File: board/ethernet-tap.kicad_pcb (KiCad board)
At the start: 4 copper layers, 399 parts, among them J1 BARREL_JACK, J10 XILINX_JTAG, J2 BEL_FUSE_0826-1G1T-23-F, J3 JUMPER_0402_SPDT, J4 JUMPER_0402_SPDT, J5 RJ45, J6 BEL_FUSE_0826-1G1T-23-F, J7 BEL_FUSE_0826-1G1T-23-F, J8 BEL_FUSE_0826-1G1T-23-F, J9 XILINX_JTAG, SW1 SWITCH, SW2 SWITCH, SW3 SWITCH, SW4 SWITCH, SW5 SWITCH, SW6 SWITCH, SW7 BUTTON, U1 LTC3374-QFN, U10 ECS-2016MVQ-250-CN-TR, U11 ECS-2016MVQ-250-CN-TR, U12 ECS-2016MVQ-250-CN-TR, U13 STM32H735-UFBGA176-25, U14 S25FLxxxS_BGA24_5x5_VIO, U2 KSZ9031RN, U3 MAX232, U4 XC7S15-1FTGB196C, U5 KSZ9031RN, U6 KSZ9031RN, U7 ECS-2016MVQ-250-CN-TR, U8 ECS-2016MVQ-250-CN-TR, U9 KSZ9031RN

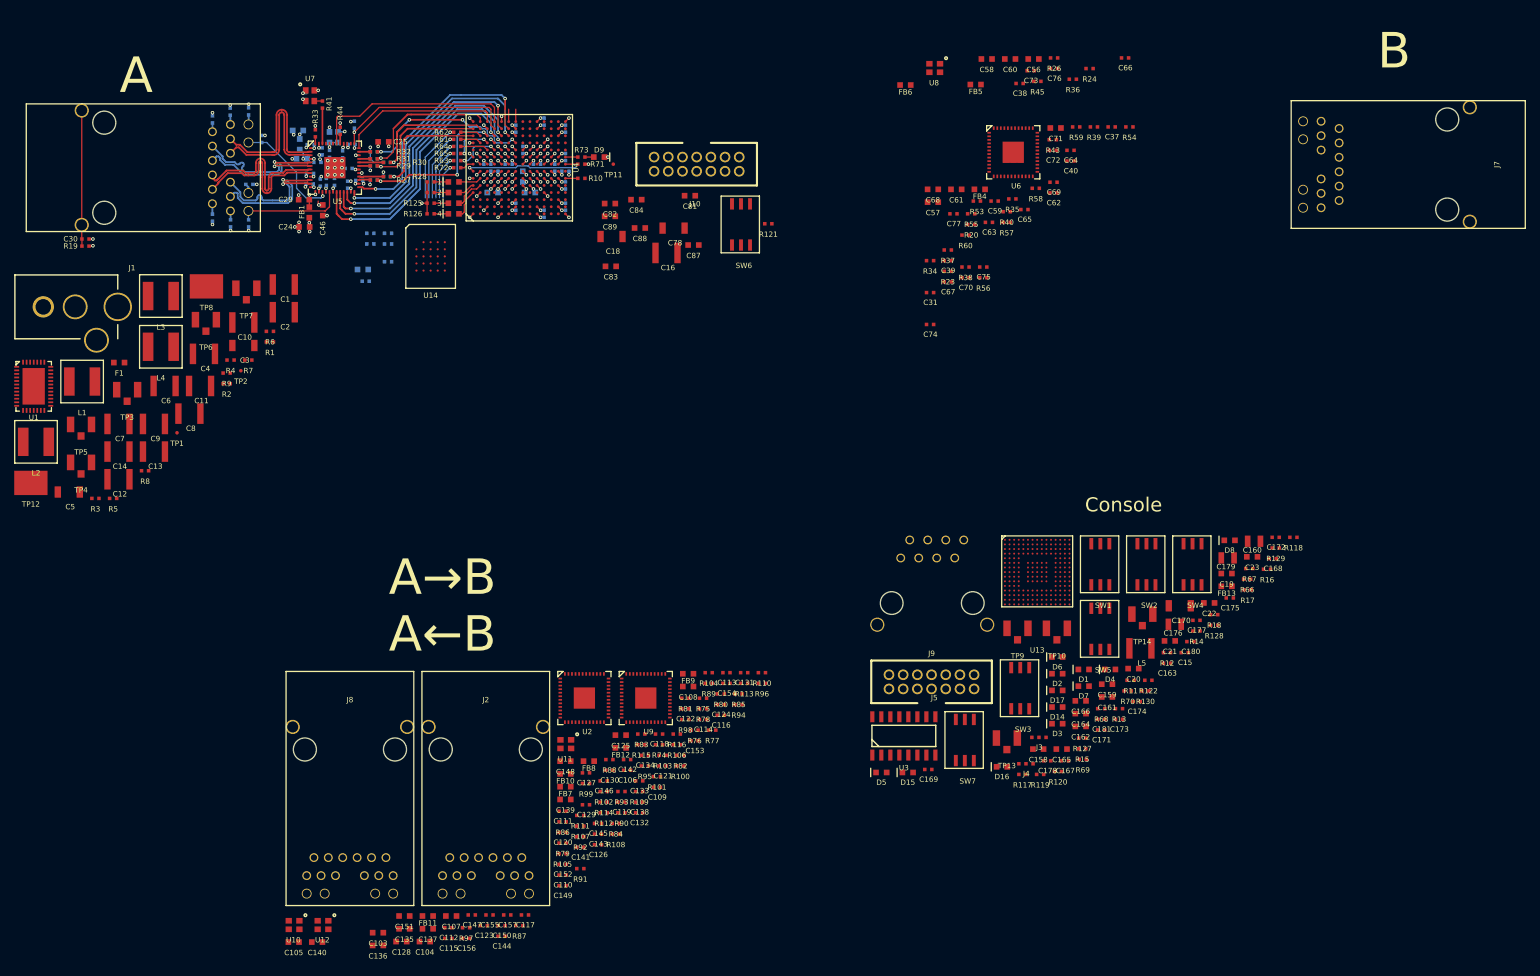
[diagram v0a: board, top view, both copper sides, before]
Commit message: Good progress hooking up second PHY
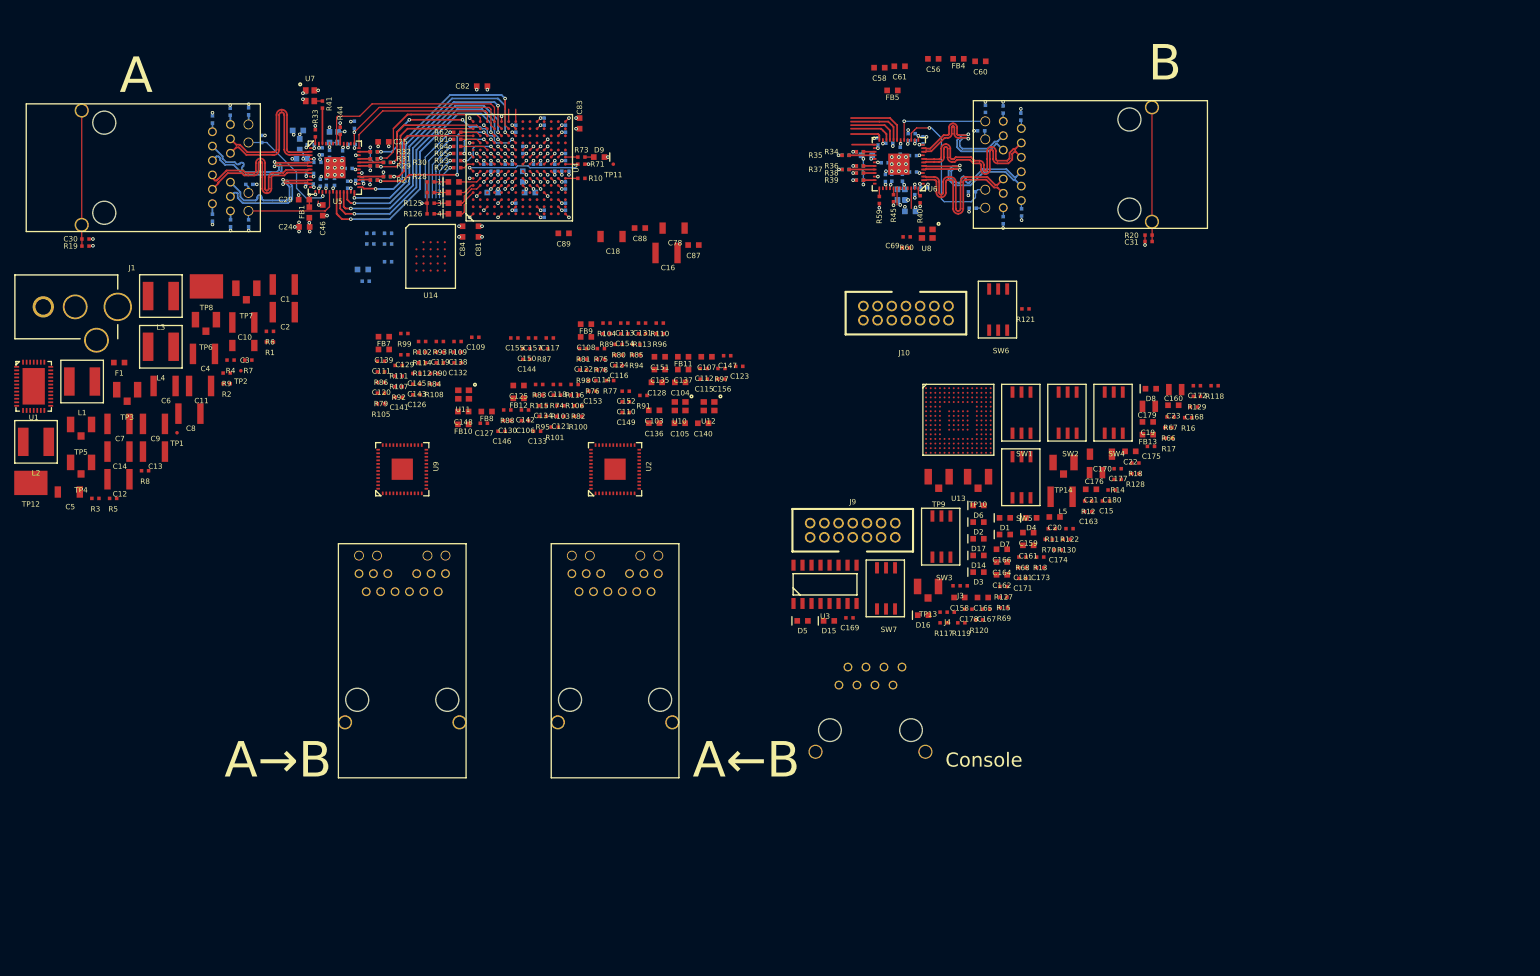
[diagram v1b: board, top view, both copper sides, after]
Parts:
- C37, C38, C39, C40, C57, C59, C62, C63, C64, C65, C66, C67, C68, C70, C71, C72, C73, C74, C75, C76, C77, FB6, R23, R24, R26, R43, R53, R54, R55, R56, R57, R58: moved to B.Cu
- moved C105 91.2 mm to (111.6, 75.0)
- moved C140 91.2 mm to (114.9, 75.0)
- moved U10 91.2 mm to (111.7, 72.6)
- moved U12 91.2 mm to (115.8, 72.6)
- moved C112 86.7 mm to (115.0, 67.3)
- moved C115 86.7 mm to (115.0, 68.8)
- moved C135 86.7 mm to (108.8, 67.5)
- moved C137 86.7 mm to (112.1, 67.5)
- moved C156 86.7 mm to (117.5, 68.8)
- moved R97 86.7 mm to (117.5, 67.3)
- moved C104 86.7 mm to (111.7, 69.2)
- moved C123 86.7 mm to (120.0, 67.0)
- moved C128 86.7 mm to (108.4, 69.2)
- moved C147 86.7 mm to (118.3, 65.5)
- moved C107 86.7 mm to (115.4, 65.7)
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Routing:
- net /GND: track 342.5 -> 481.9 mm, vias 102 -> 135
- net /3V3: track 154.4 -> 242.9 mm, vias 26 -> 37
- net /1V2: track 36.5 -> 66.2 mm, vias 9 -> 17
- net /Thru Path/ETH1_A_P: track 0.00 -> 24.8 mm
- net /Thru Path/ETH1_A_N: track 0.00 -> 24.8 mm
- net /Thru Path/ETH1_C_P: track 0.00 -> 24.8 mm
- net /Thru Path/ETH1_C_N: track 0.00 -> 24.8 mm
- net /Thru Path/ETH1_LED2_N: track 0.00 -> 22.2 mm, vias 0 -> 1
- net /Thru Path/ETH1_B_N: track 0.00 -> 20.7 mm, vias 0 -> 1
- net /Thru Path/ETH1_B_P: track 0.00 -> 20.6 mm, vias 0 -> 1
- net /Thru Path/ETH1_D_N: track 0.00 -> 20.3 mm, vias 0 -> 1
- net /Thru Path/ETH1_D_P: track 0.00 -> 19.1 mm, vias 0 -> 1
- net Net-(C31-Pad2): track 0.00 -> 18.9 mm
- net /Thru Path/ETH1_LED1_N: track 0.00 -> 14.1 mm, vias 0 -> 1
- net /Thru Path/ETH1_A3V3: track 0.00 -> 9.28 mm, vias 0 -> 3
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
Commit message: Continued initial layout. Good progress on monitor port PHYs.
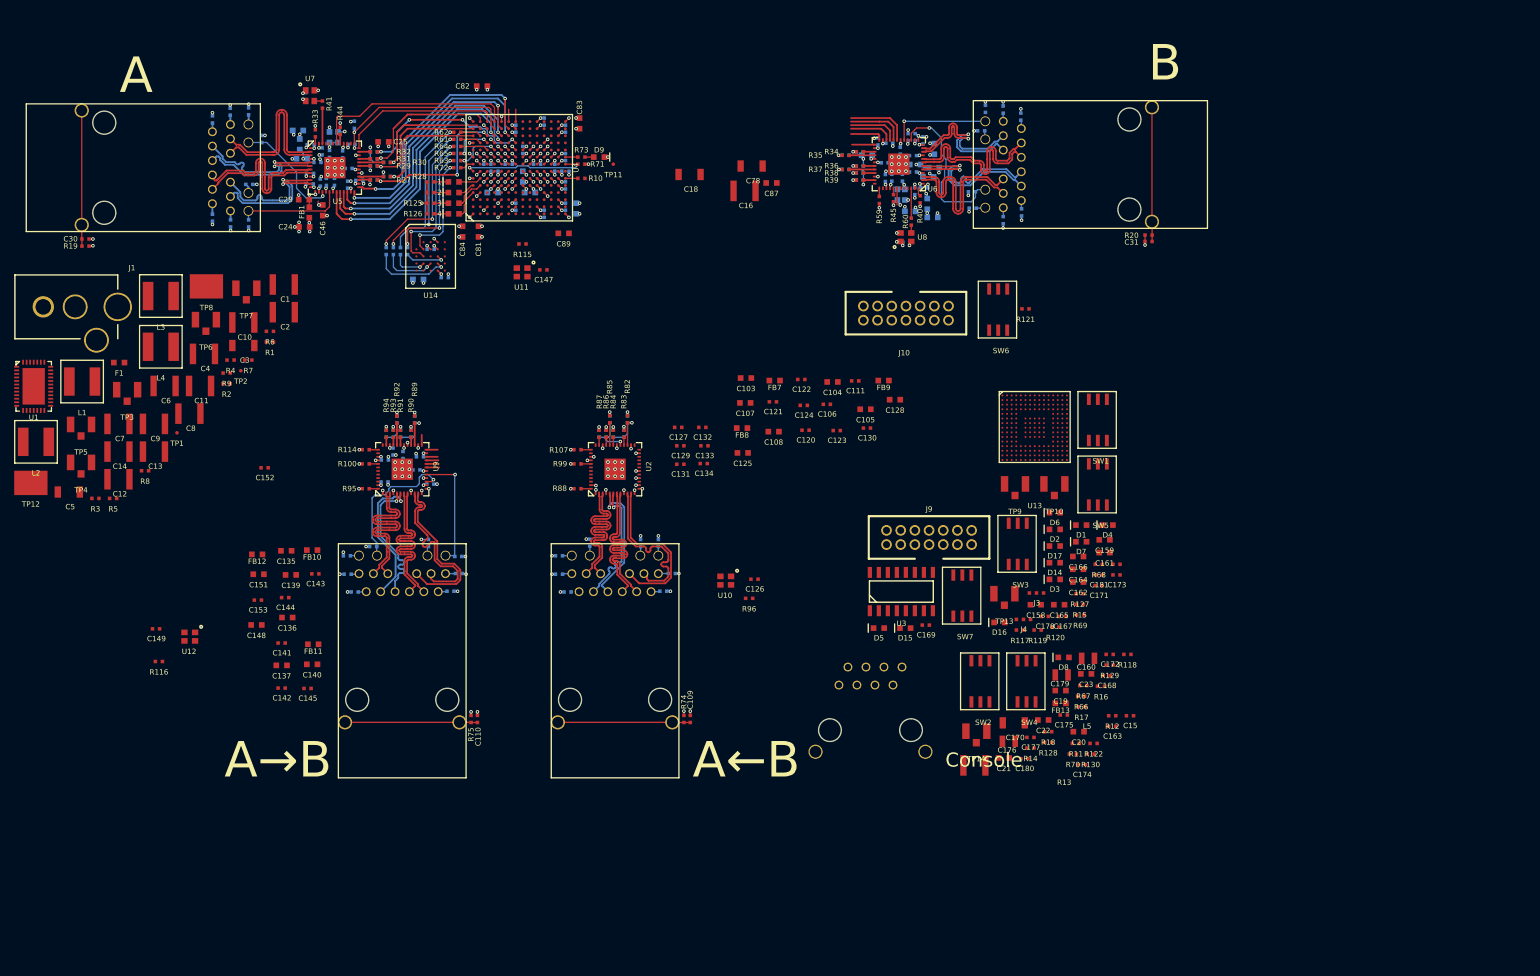
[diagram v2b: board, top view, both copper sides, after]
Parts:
- C112, C113, C114, C115, C116, C117, C118, C119, C138, C146, C150, C154, C155, C156, C157, C56, C58, C60, C61, C69, C88, FB4, FB5, R101, R102, R103, R104, R105, R106, R108, R109, R110, R111, R112, R113, R76, R77, R78, R79, R80, R81, R97, R98: moved to B.Cu
- moved U12 80.1 mm to (42.5, 105.1)
- moved C149 72.9 mm to (37.8, 104.0)
- moved R116 70.4 mm to (38.2, 108.6)
- moved C137 70.3 mm to (55.5, 109.2)
- moved C111 66.9 mm to (136.3, 69.0)
- moved FB11 66.0 mm to (60.0, 106.2)
- moved C140 64.8 mm to (59.8, 109.0)
- moved C151 64.3 mm to (52.2, 96.3)
- moved C109 61.7 mm to (113.1, 116.7), turned to -90 degrees
- moved C120 60.2 mm to (129.3, 76.0)
- moved C135 58.5 mm to (56.1, 93.0)
- moved C136 58.5 mm to (56.3, 102.4)
- moved C153 55.6 mm to (52.1, 100.0)
- moved FB7 55.4 mm to (125.0, 69.0)
- moved R75 55.3 mm to (82.2, 116.7), turned to -90 degrees
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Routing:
- net /GND: track 481.9 -> 698.7 mm, vias 135 -> 188
- net /3V3: track 242.9 -> 390.2 mm, vias 37 -> 63
- net /1V2: track 66.2 -> 110.9 mm, vias 17 -> 30
- net /Monitor Path/ETH3_D_N: track 0.00 -> 24.0 mm
- net /Monitor Path/ETH3_D_P: track 0.00 -> 24.0 mm
- net /Monitor Path/ETH3_A_P: track 0.00 -> 23.9 mm
- net /Monitor Path/ETH3_A_N: track 0.00 -> 23.9 mm
- net /Monitor Path/ETH3_C_N: track 0.00 -> 23.9 mm
- net /Monitor Path/ETH3_C_P: track 0.00 -> 23.9 mm
- net /Monitor Path/ETH2_D_N: track 0.00 -> 23.1 mm
- net /Monitor Path/ETH2_D_P: track 0.00 -> 23.0 mm
- net /Monitor Path/ETH2_C_N: track 0.00 -> 22.9 mm
- net /Monitor Path/ETH2_C_P: track 0.00 -> 22.9 mm
- net /Monitor Path/ETH2_A_P: track 0.00 -> 22.9 mm
- net /Monitor Path/ETH2_A_N: track 0.00 -> 22.9 mm
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
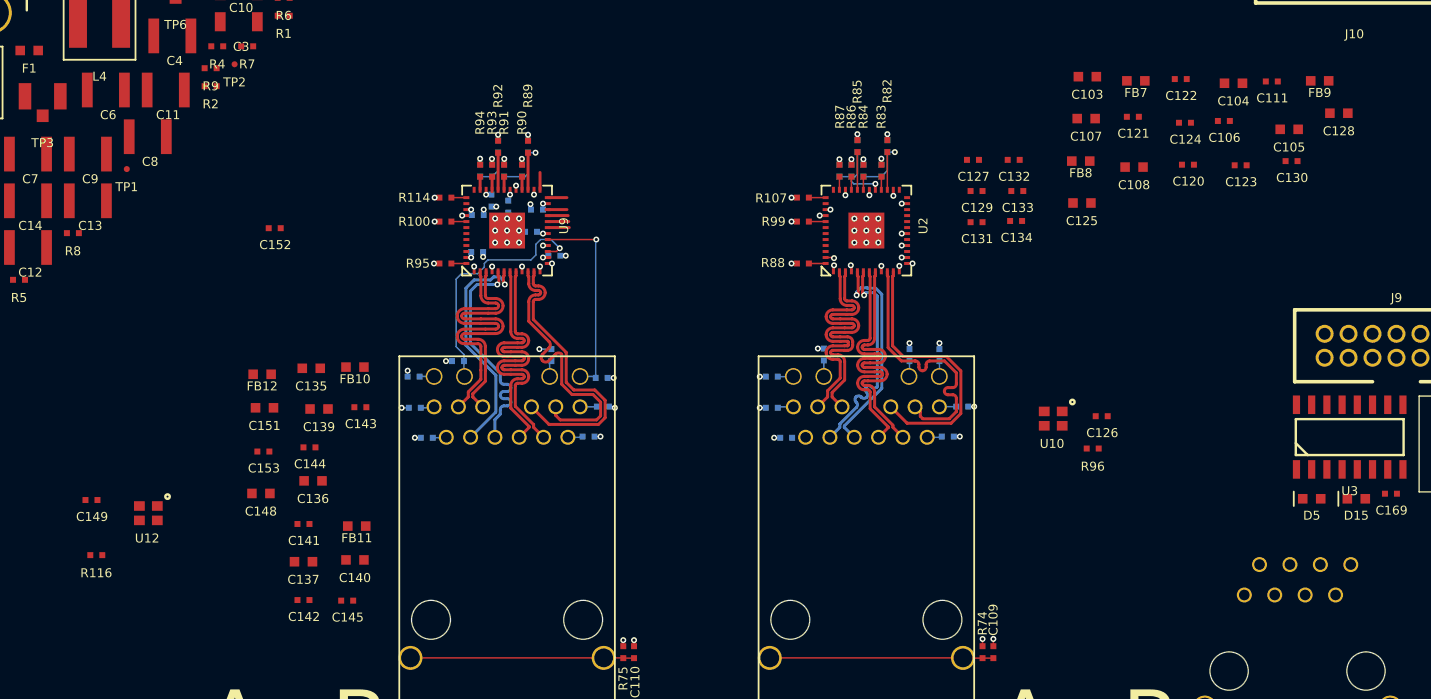
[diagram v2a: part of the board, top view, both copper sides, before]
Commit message: Continued work on monitor port PHY layout
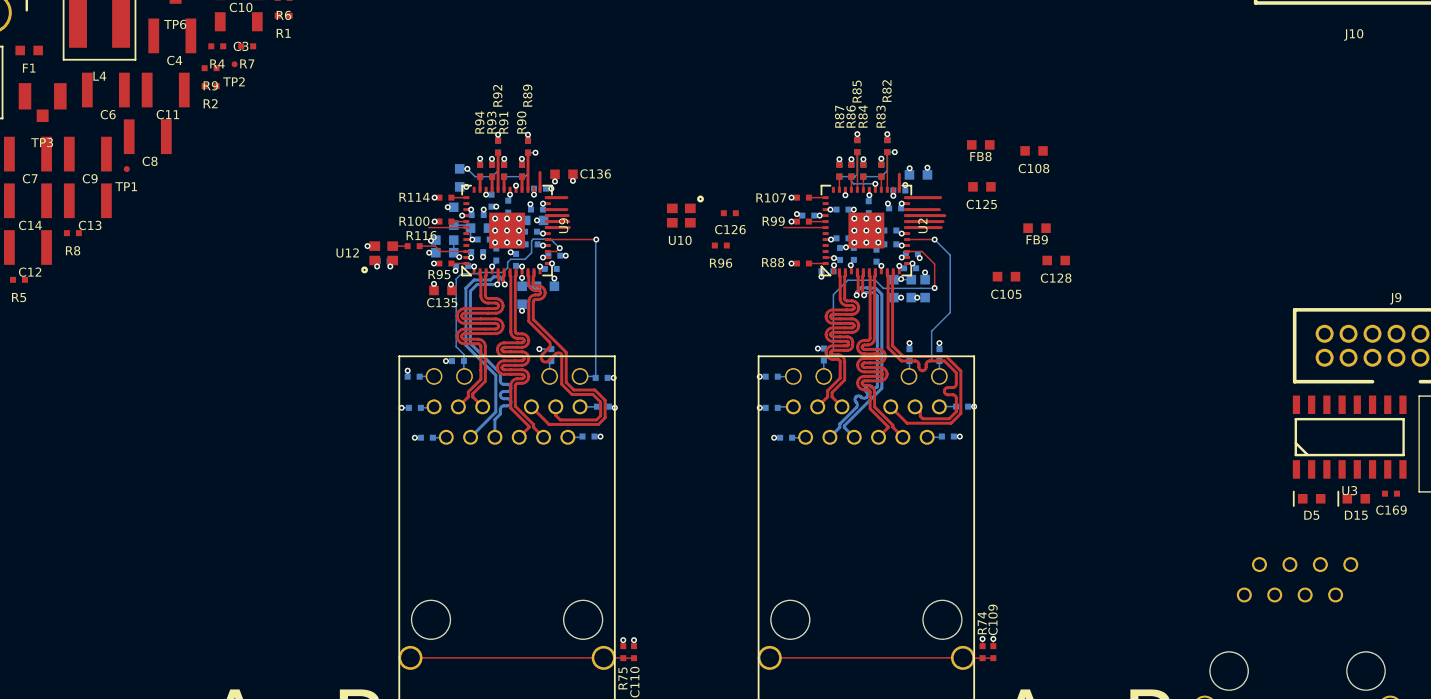
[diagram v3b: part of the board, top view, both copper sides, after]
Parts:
- C103, C104, C106, C107, C111, C120, C121, C122, C123, C124, C127, C129, C130, C131, C132, C133, C134, C137, C139, C140, C141, C142, C143, C144, C145, C148, C149, C151, C152, C153, FB10, FB11, FB12, FB7: moved to B.Cu
- moved C111 40.3 mm to (97.7, 80.2), turned to 180 degrees
- moved C130 38.1 mm to (100.5, 82.2)
- moved R116 37.0 mm to (64.7, 82.8), turned to 180 degrees
- moved C126 35.4 mm to (91.1, 80.0)
- moved R96 35.4 mm to (90.3, 82.8)
- moved U10 35.4 mm to (87.0, 80.2)
- moved C137 34.6 mm to (68.5, 77.1), turned to 90 degrees
- moved C122 33.6 mm to (99.2, 84.9), turned to 180 degrees
- moved C142 33.5 mm to (73.2, 84.0), turned to 90 degrees
- moved C123 33.1 mm to (101.5, 83.5), turned to 90 degrees
- moved C136 33.1 mm to (77.2, 76.8)
- moved C148 32.3 mm to (74.8, 80.7), turned to 180 degrees
- moved C149 31.5 mm to (62.2, 84.0)
- moved C145 31.5 mm to (71.6, 83.5), turned to 90 degrees
- moved C124 30.8 mm to (100.3, 83.5), turned to 90 degrees
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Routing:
- net /GND: track 698.7 -> 750.4 mm, vias 188 -> 207
- net /3V3: track 390.2 -> 417.5 mm, vias 63 -> 70
- net /Monitor Path/ETH2_LED2_N: track 1.33 -> 21.1 mm, vias 0 -> 1
- net /Monitor Path/ETH2_LED1_N: track 1.28 -> 15.5 mm, vias 0 -> 1
- net /Monitor Path/ETH3_CLK_25MHZ: track 0.00 -> 4.09 mm
- net /Monitor Path/ETH3_A1V2: track 3.30 -> 7.34 mm, vias 2 -> 3
- net /1V2: track 110.9 -> 114.6 mm, vias 30 -> 34
- net /Monitor Path/ETH2_RST_N: track 0.00 -> 3.50 mm
- net /Monitor Path/ETH3_A1V2_PLL: track 0.00 -> 3.47 mm, vias 0 -> 1
- net /Monitor Path/ETH3_A3V3: track 8.17 -> 11.4 mm, vias 3 -> 4
- net /Monitor Path/ETH3_RST_N: track 0.00 -> 3.15 mm
- net /Monitor Path/ETH2_RGMII_TXD2: track 0.00 -> 3.15 mm
- net /Monitor Path/ETH2_RGMII_TXD1: track 0.00 -> 3.00 mm
- net /Monitor Path/ETH2_RGMII_TXD0: track 0.00 -> 2.85 mm
- net /Monitor Path/ETH2_RGMII_TX_CLK: track 0.00 -> 2.80 mm
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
